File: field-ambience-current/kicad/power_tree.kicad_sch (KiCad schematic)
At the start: 13 parts, among them J1 USB_C_Receptacle (TYPE-C-31-M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, U5 AP7361C-33 1A LDO (+5V->+3V3,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

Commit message: kicad(gen): flow the 5 sourcing-fix part swaps into the generator (r18.71)
The generator is the schematic's source of truth, so the BOM part swaps must
live here (previously only in BOM/HTML). Swapped LCSC + MPN in the generator,
regenerated the .kicad_sch, re-exported jlc_bom.csv:
- FB2 ferrite C84094 -> C19330 (same Murata MPN, JLC 950k)
- VCAP C24539 -> C23630 (2.2uF 16V X5R 0603, JLC Basic)
- charger LED C72041 (blue+EOL!) -> C965800 (orange 605nm 0603)
- C_BULK2 C2880380 (stock 1) -> C23742 (100uF 10V X5R 1210)
- modifier buttons SW6-10 C2845240 (stock 30) -> C36498965 (HX B3F square
  head); footprint SW_TC1212-7.3_THT_4P reused, HX pinout verify noted in FP_NOTE.

The generated schematic Aron opens now carries the correct in-stock parts.
check_pinmap passes; jlc_bom.csv has the new codes (old ones gone).

Co-Authored-By: Claude Opus 4.8 <noreply@anthropic.com>
Claude-Session: https://claude.ai/code/session_01K5kLTFpDCCoYwx2dq6RkAv
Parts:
- C_BULK2: LCSC C2880380 -> C23742; MPN LMK325ABJ107MM-T (Taiyo Yuden, 100uF 10V X5R) -> CL32A107MPVNNNE (Samsung, 100uF 10V X5R)
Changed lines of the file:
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@@
       (property "Datasheet" "~" (at 73 63.81 0)
         (effects (font (size 1.27 1.27)) hide))
-      (property "MPN" "LMK325ABJ107MM-T (Taiyo Yuden, 100uF 10V X5R)" (at 75.54 67.62 0)
+      (property "MPN" "CL32A107MPVNNNE (Samsung, 100uF 10V X5R)" (at 75.54 67.62 0)
         (effects (font (size 1.27 1.27)) hide))
-      (property "LCSC" "C2880380" (at 75.54 68.89 0)
+      (property "LCSC" "C23742" (at 75.54 68.89 0)
         (effects (font (size 1.27 1.27)) hide))
     (instances

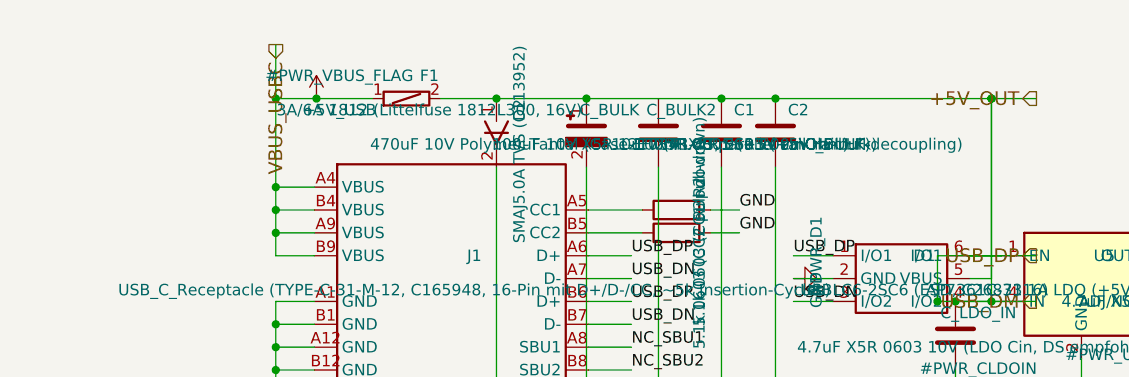
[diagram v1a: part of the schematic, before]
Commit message: fix(power): electrical audit — 3 critical boost/power-path bugs (r18.79) (#91)
User asked for a components+connections review (no mechanics), looking for
critical errors. Systematic electrical audit of the generated schematics:
hier-label<->root-pin matching, root wiring connectivity (union-find over
wire endpoints + label-name merging), dangling nets, duplicate refdes, I2C
addresses, pull-ups, and the boost converter checked line-by-line against
the TI TPS61089 datasheet (SLVSD38C -- equations read from rendered PDF
pages, not from memory).

CRITICAL FIX 1 -- boost FB divider set the "+5V" rail to 7.43V:
R23/R24 = 200k/39k with VREF 1.212V (TI EC table) gives VOUT = 7.43V, not
5V. That would have destroyed the PAM8403 amp (5.5V abs max) and the
planned TPS22918 load switch (5.5V max) at first power-on, and overstressed
the AP7361C LDO (6V max). Fix: R23 = 121k (0603WAF1213T5E, C25809, live-
verified, 71k stock) -> VOUT = 4.97V per DS Eq. 5. (122k for exactly 5.00V
has no verifiable LCSC stock; -0.6% errs in the safe direction.)

CRITICAL FIX 2 -- R_ILIM 20k = 51.5A current limit (i.e. none):
TI Eq. 4: ILIM = 1,030,000 / R_ILIM. The generator comment claimed "20k ->
~4A peak"; the real result is 51.5A -- effectively no current limit, with
the inductor (Isat min 6.75A) unprotected under fault. Fix: R_ILIM = 174k
(0603WAF1743T5E, C22890, live-verified) -> 5.92A typ / 5.12A min (above the
~4.7A worst-case operating peak) / ~6.7A max (below Isat-min 6.75A).

CRITICAL FIX 3 -- Q1 power-path back-feed + fuse bypass:
Q1 (P-FET, S=VBUS pre-fuse, D=+5V rail, G->GND) plus power_tree exporting
the rail directly behind F1 meant: with no USB plugged in, the boost's 5V
back-fed VBUS through Q1's body diode (and in parallel through F1 -- PTC
fuses conduct both ways), pulling the gate-source negative and latching Q1
fully on. Consequences: the charger (VDD = VBUS_USBC) charged the battery
from its own boost output -- a self-discharge loop draining the battery at
~1.5x the charge cu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
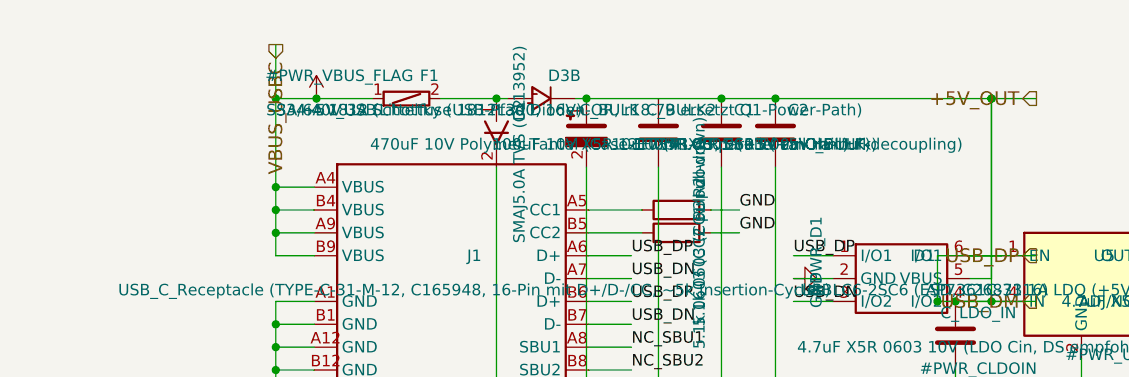
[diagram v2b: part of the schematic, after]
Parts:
- added D3B: SS34 40V 3A Schottky (USB-Pfad Dioden-OR, r18.79 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, Diode_SMD:D_SMA, symbol Device:D_Schottky
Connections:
- net +5V_OUT: now also D3B.1 (K); no longer D2.1 (K), F1.2
- new net: D2.1 (K), D3B.2 (A), F1.2
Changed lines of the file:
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@@
     (company "Field Ambience Project")
     (comment 1 "Per SPEC v0.6.3 §1 + §3")
-    (comment 2 "USB-C → F1(3A/6A) → C_BULK(470µF Polymer + 220µF MLCC) → +5V rail")
+    (comment 2 "USB-C → F1(3A/6A) → D3B SS34 (r18.79 Dioden-OR) → +5V rail (C_BULK 470µF Polymer + 100µF MLCC)")
     (comment 3 "USB-C VBUS/GND-Pin-Belegung per USB Type-C Spec Rev 2.1 (v0.6.3 fix)")
     (comment 4 "ESD: USBLC6-2SC6 on D+/D-; TVS: SMAJ5.0A on +5V"))
@@
       (project "field_ambience"
         (path "/8f124281-8f89-47ab-aa39-bcbf8f1e5e4d" (reference "#PWR_VBUS_FLAG") (unit 1)))))
+  (symbol (lib_id "Device:D_Schottky") (at 60 60.0 180) (unit 1)
+    (in_bom yes) (on_board yes) (dnp no)
+      (property "Reference" "D3B" (at 62.54 57.46 0)
+        (effects (font (size 1.27 1.27))))
+      (property "Value" "SS34 40V 3A Schottky (USB-Pfad Dioden-OR, r18.79 ersetzt Q1-Power-Path)" (at 62.54 61.27 0)
+        (effects (font (size 1.27 1.27))))
+      (property "Footprint" "Diode_SMD:D_SMA" (at 60 60.0 0)
+        (effects (font (size 1.27 1.27)) hide))
+      (property "Datasheet" "~" (at 60 60.0 0)
+        (effects (font (size 1.27 1.27)) hide))
+      (property "MPN" "SS34" (at 62.54 63.81 0)
+        (effects (font (size 1.27 1.27)) hide))
+      (property "LCSC" "C8678" (at 62.54 65.08 0)
+        (effects (font (size 1.27 1.27)) hide))
+    (instances
+      (project "field_ambience"
+        (path "/8f124281-8f89-47ab-aa39-bcbf8f1e5e4d" (reference "D3B") (unit 1)))))
   (symbol (lib_id "Device:CP") (at 65 63.81 0) (unit 1)
     (in_bom yes) (on_board yes) (dnp no)
@@
     (stroke (width 0) (type default))
 )
-  (wire (pts (xy 55 60.0) (xy 65 60.0))
-    (stroke (width 0) (type default))
-)
+  (wire (pts (xy 55 60.0) (xy 56.19 60.0))
+    (stroke (width 0) (type default))
+)
+  (wire (pts (xy 63.81 60.0) (xy 65 60.0))
+    (stroke (width 0) (type default))
+)

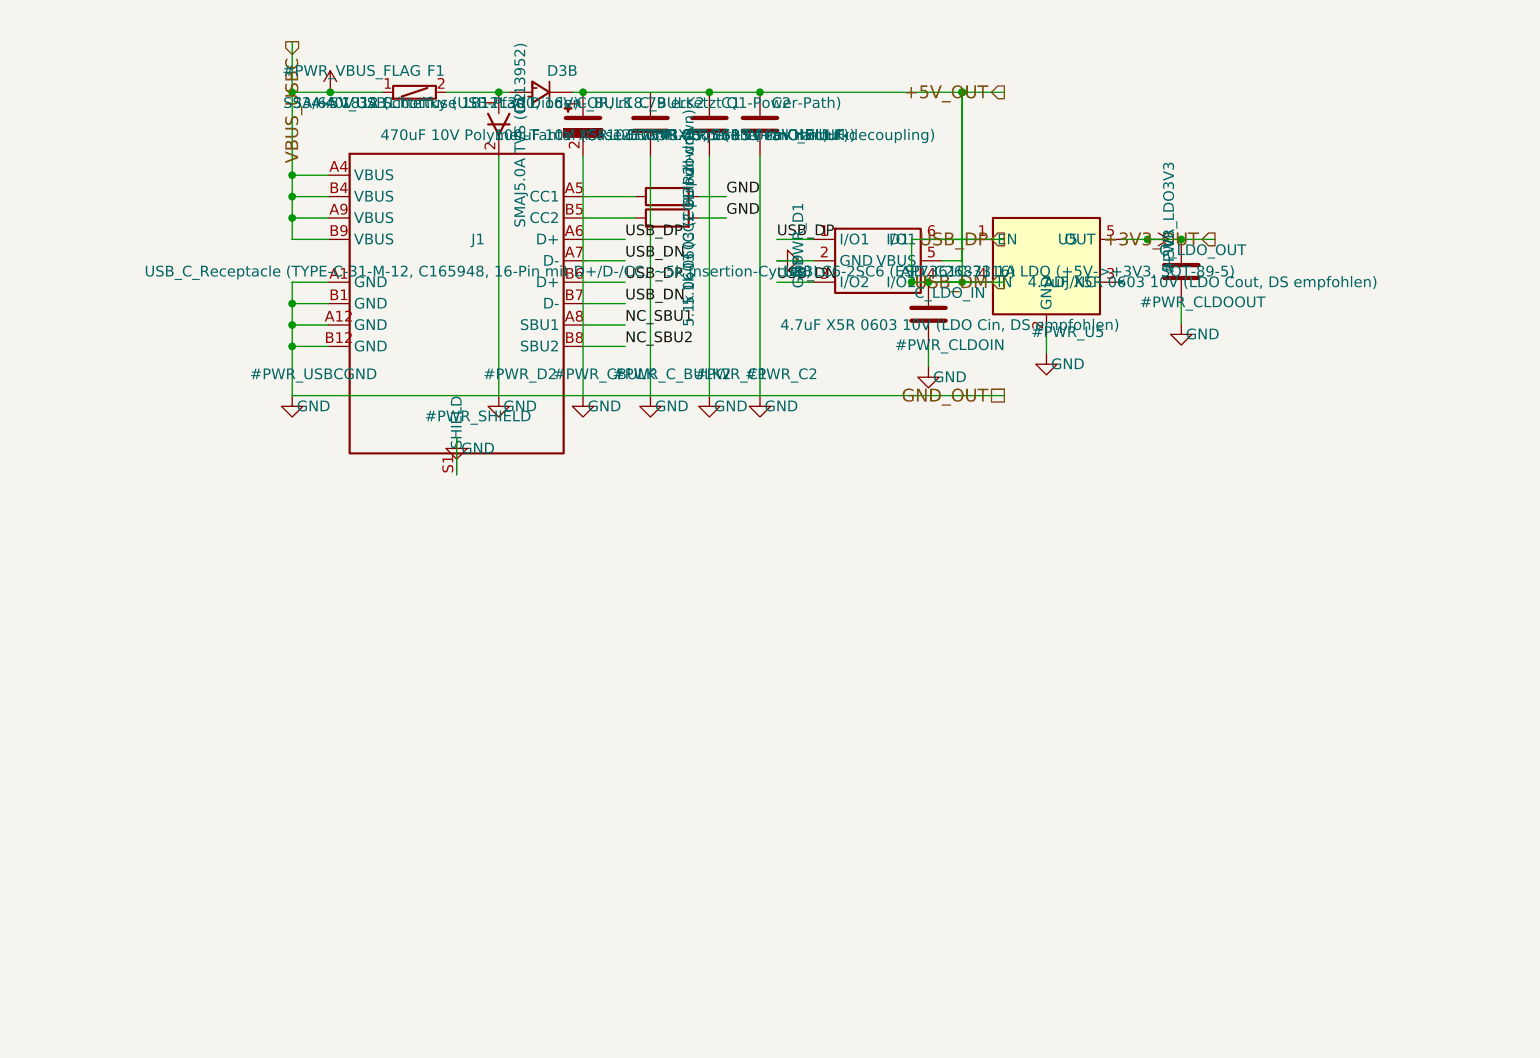
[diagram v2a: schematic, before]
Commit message: fix(pcb): geometric pin-level ERC — 7 copper shorts, 4 open circuits, boost loop instability (r18.80) (#92)
Headless geometric ERC (every pin anchor vs every wire segment, union-find
net build, hier-label/root-pin matching) over all 7 sheets found 12 real
defects; each verified in generator source and fixed there.

Copper shorts (pin/label anchors landing on foreign wires):
- power_tree: USB D+ AND D- hard-shorted to +5V — the U5 LDO block sat in
  the USB data corridor (EN pin on the DP wire, IN pin on the DM wire,
  rail drop overlapping the ESD VBUS wire). Block moved to (130,130).
- mcp: I2C_SCL shorted to GND — C5's GND pin landed exactly on the SCL
  wire (VDD pin 9 and SCL pin 12 are exactly 3 grid rows = 7.62mm apart,
  the cap's pin pitch). Entire I2C bus (U2+U6+U10) was dead. C5/C5b moved.
- audio: PCM_XSMT and I2S_LRCK shorted to GND (same 7.62mm trap, C8a/C8b
  and C_LDOO) — DAC permanently muted / no word clock. Caps flipped up.
- stm32: BOOT0 permanently HIGH twice over (+3V3 flag placed on the BOOT0
  node point; SW_BOOT wire drawn through its own pin-2 anchor) — MCU would
  always enter the ROM bootloader, never firmware.
- stm32: VDDA copper-tied to VDD (pin-21 stub drawn through the VDD pin-100
  anchor), bypassing FB2.
- battery: U8_SW_NODE label sat on the SW/BOOT wire crossing, merging the
  bootstrap net with the switch node (C_BOOT ineffective).

Open circuits:
- lcd: J3 LCD header — all 8 pins floating (wiring assumed KiCad-standard
  pins at -5.08 left; custom lib has pins at +3.81 right). J3 rotated 180.
- stm32: J4 SWD header — all 3 pins floating (same assumption). Board was
  unprogrammable.
- stm32: FB2 rotated 90 off its wires — both pins floating (VDDA had no
  intended supply path).
- stm32: lib_symbols entry lacked the MCU: prefix — KiCad cannot resolve
  U1 at all (exact lib_id match required).

Boost control loop (TPS61089, TI SLVSD38C eqs 15/17/18, validated by
reproducing TI's own 9V/2A reference values):
- R_COMP 22k -> 6.2k (n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
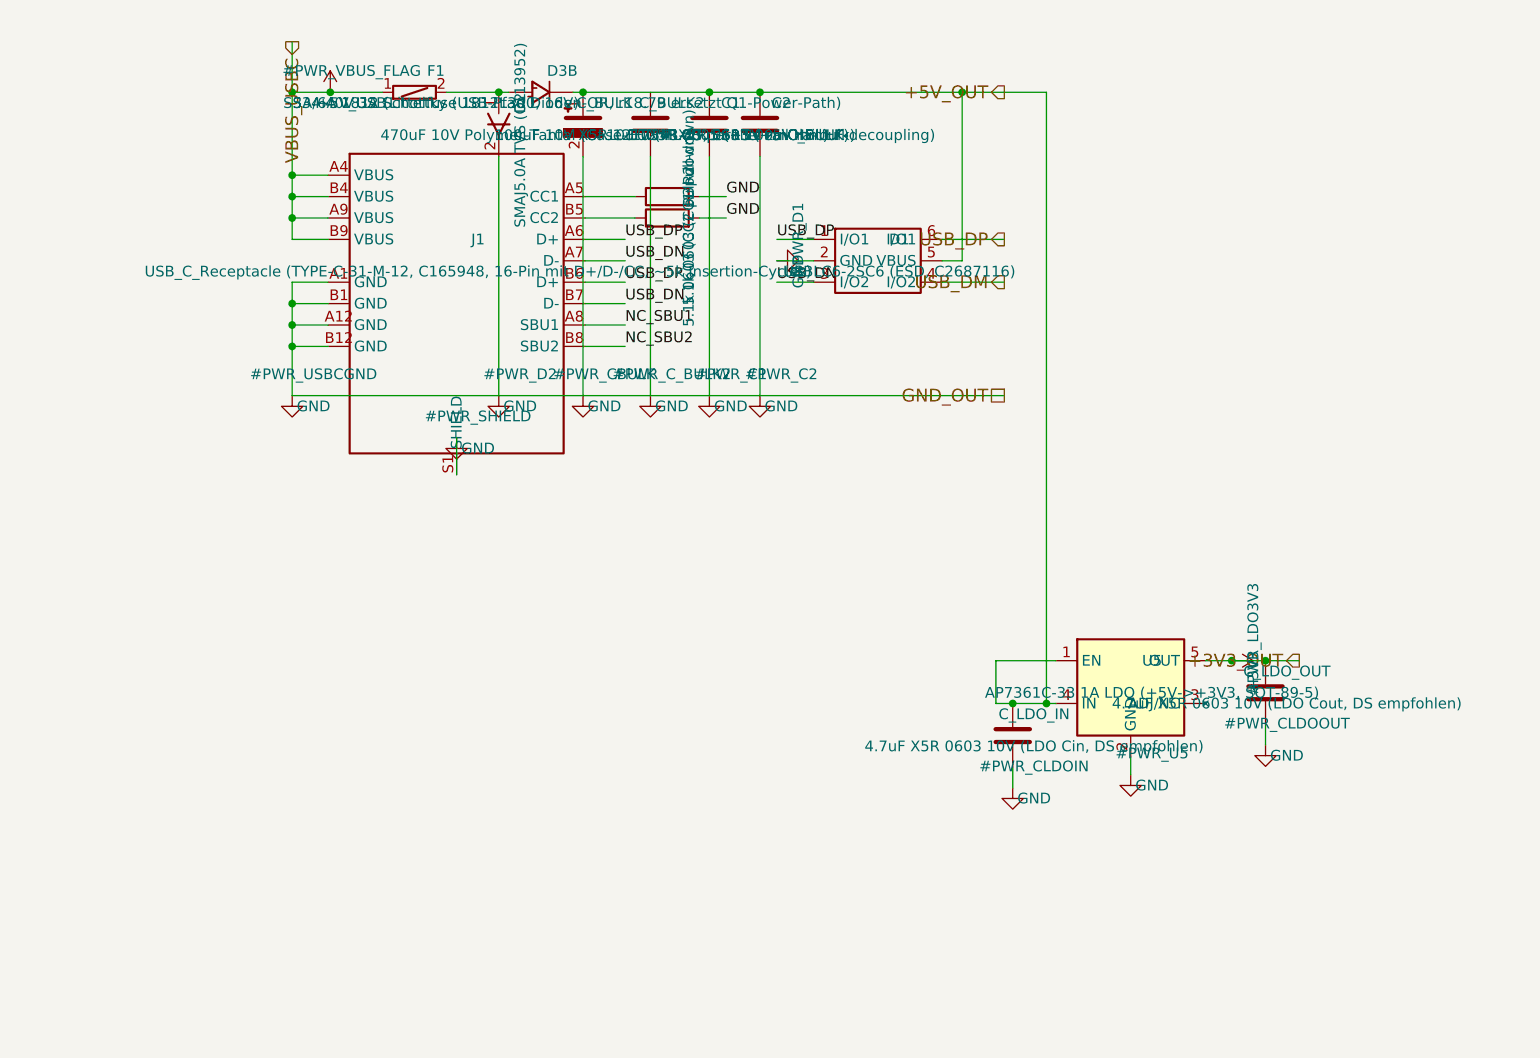
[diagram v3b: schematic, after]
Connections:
- net +5V_OUT: no longer D1.1 (I/O1), D1.4 (I/O2), D1.6 (I/O1), J1.A6 (D+), J1.B6 (D+)
- new net USB_DM: D1.4 (I/O2)
- new net USB_DP: D1.1 (I/O1), D1.6 (I/O1), J1.A6 (D+), J1.B6 (D+)
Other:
- moved on the sheet: C_LDO_IN, C_LDO_OUT, U5

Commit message: feat(pcb): ADR-0016 power-off block wired in + global +5V net bridged; SW_PWR side-mount datasheet-verified (r18.81)
Triggered by the user's question whether the MST-12D18G3 on/off switch can
be operated from the side on a horizontal PCB.

Answer (verified against the SHOU HAN datasheet drawing, LCSC PDF p.1):
YES — the body sits flat on the board (3 SMD legs + 2 locator pegs), the
slider stem protrudes HORIZONTALLY 3mm past the body on the side opposite
the pins, window z ~2.3-3.8mm above the board, 2mm travel at 200gf lateral.
Place at the board edge, slot in the enclosure side wall. The vendored
footprint matches the official MSK12D land pattern exactly (3 pads 1.2mm
at 2.5mm pitch, 0.9mm peg holes 6.8mm apart, 3.2mm offset). Open item for
fab: terminal mapping (common = middle pad) is the SPDT convention but the
datasheet does not label terminals — buzz out before ordering; the wrong
case is fail-safe (unit simply won't switch on, PWR_ON stays pulled low).

The question exposed two critical gaps:

1. The ADR-0016 power-off block (decided 2026-06-27, pin-level spec in the
   ADR, listed in BOM docs/HTML) was NEVER drawn into the schematic — the
   generator and jlc_bom.csv had no U_PWR/SW_PWR at all: the board would
   have shipped without any on/off switch. Now wired in power_tree:
   +5V_RAIL -> U_PWR (TPS22918, C131941 live-verified) -> +5V_SW -> LDO
   VIN; SW_PWR common -> PWR_ON = U_PWR.ON, throw A -> +5V rail, R_PWR_PD
   100k default-OFF, C_UPWR_IN 1uF (TI DS pin-1 note), C_PWR_SW 10uF.
   Charger stays ahead of the switch (dark, but charging). Two ADR pin
   errors corrected against TI SLVSD76C: pin 4 is CT (not NC; floating is
   DS-sanctioned = fastest rise, CT cap = optional soft-start), and
   floating QOD would DISABLE quick discharge - QOD is tied to VOUT
   (DS option 2, active discharge of the switched domain at power-off).
   New lib symbols Power_Switch:TPS22918 and Switch:SW_SPDT.

2. The global +5V power-symbol net was a sourceless island: no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
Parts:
- added C_PWR_SW: 10uF X5R 0805 (+5V_SW output cap, ADR-0016), Capacitor_SMD:C_0805_2012Metric, symbol Device:C
- added C_UPWR_IN: 1uF X5R 0603 (TPS22918 VIN bypass, DS Pin-1-Note), Capacitor_SMD:C_0603_1608Metric, symbol Device:C
- added R_PWR_PD: 100k 0603 (PWR_ON pull-down, Default AUS), Resistor_SMD:R_0603_1608Metric, symbol Device:R
- added SW_PWR: MST-12D18G3 slide switch (Haupt-Aus, side-actuate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, field_ambience:SW_MST-12D18_SlideSwitch_RA, symbol Switch:SW_SPDT
- added U_PWR: TPS22918DBVR load switch (+5V_RAIL -> +5V_SW, ADR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, Package_TO_SOT_SMD:SOT-23-6, symbol Power_Switch:TPS22918
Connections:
- net GND: now also C_PWR_SW.2, C_UPWR_IN.2, R_PWR_PD.2, U_PWR.2 (GND)
- net +5V_OUT renamed +5V
- net +5V: now also C_UPWR_IN.1, SW_PWR.1 (A), U_PWR.1 (VIN); no longer C_LDO_IN.1, U5.1 (EN), U5.4 (IN)
- new net +5V_SW: C_LDO_IN.1, C_PWR_SW.1, U5.1 (EN), U5.4 (IN), U_PWR.5 (QOD), U_PWR.6 (VOUT)
- new net NC_SW_PWR_B: SW_PWR.3 (B)
- new net PWR_ON: R_PWR_PD.1, SW_PWR.2 (COM), U_PWR.3 (ON)
